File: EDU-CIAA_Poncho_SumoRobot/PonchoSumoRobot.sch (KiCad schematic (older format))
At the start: 26 parts, among them K1 RELAY_C, K2 RELAY_C, K3 RELAY_C, K4 RELAY_C, P1 CONN_01X02, P3 CONN_02X09, P4 CONN_01X02, P5 CONN_01X02, Q1 BC817-40, Q2 BC817-40, Q3 BC817-40, Q4 BC817-40

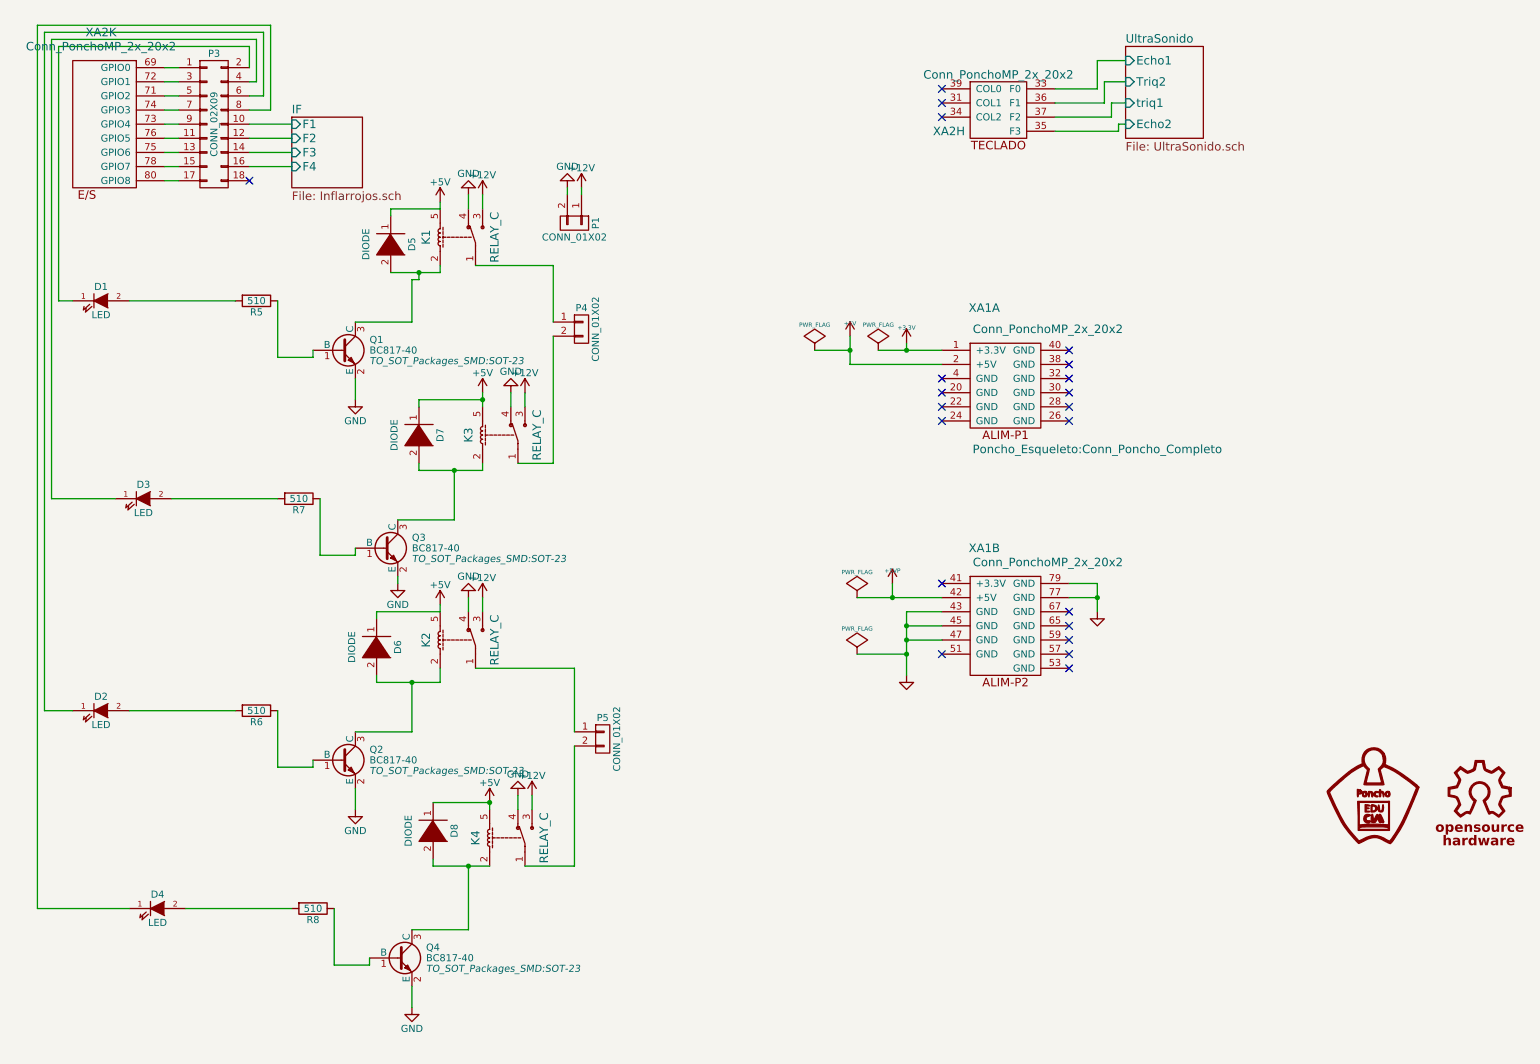
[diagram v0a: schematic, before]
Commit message: Reorganizo bibliotecas en esquemático y PCB. Reparo señal de 12V. Agrego Footprints. Coloco plantilla EDU-CIAA. Reparo asociación conector EDU-CIAA en sch y pcb.
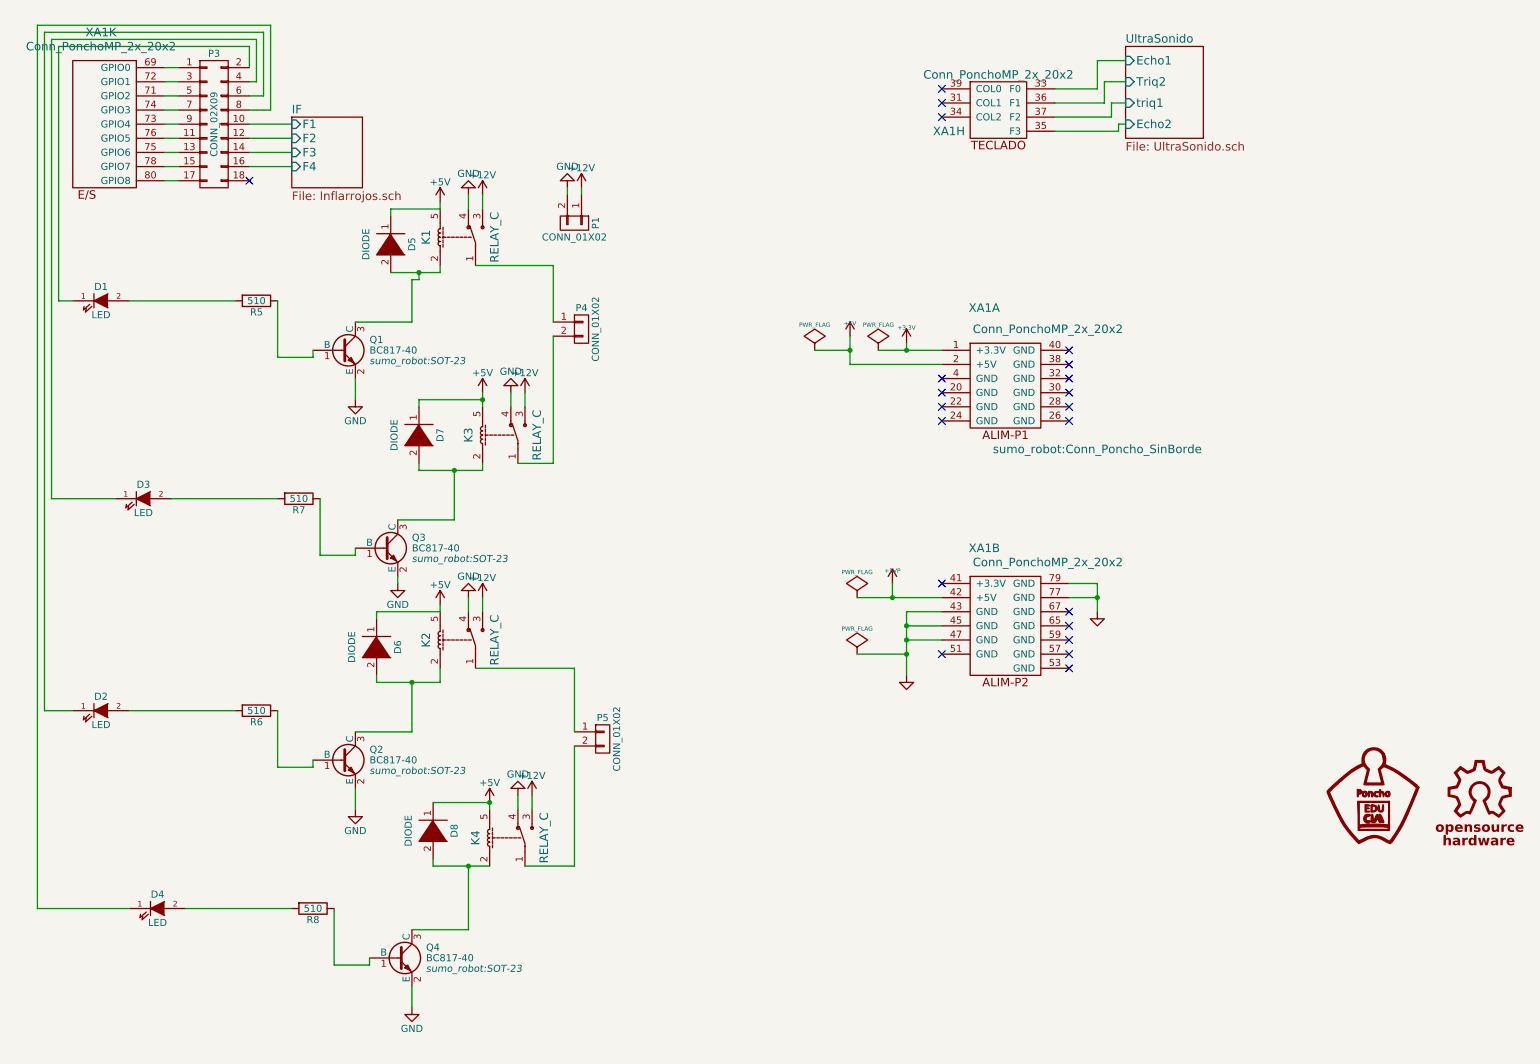
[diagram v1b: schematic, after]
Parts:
- D1, D2, D3, D4: footprint LEDs:LED_1206 -> sumo_robot:LED_1206
- D5, D6, D7, D8: footprint Diodes_ThroughHole:Diode_DO-41_SOD81_Horizontal_RM10 -> sumo_robot:Diode_DO-41_SOD81_Horizontal_RM10
- K1, K2, K3, K4: footprint Relays_ThroughHole:Relay_SANYOU_SRD_Series_Form_C -> sumo_robot:Relay_SANYOU_SRD_Series_Form_C
- P1, P4, P5: footprint Connect:bornier2 -> sumo_robot:bornier2
- P3: footprint Pin_Headers:Pin_Header_Straight_2x09 -> sumo_robot:Pin_Header_Straight_2x09
- Q1, Q2, Q3, Q4: footprint TO_SOT_Packages_SMD:SOT-23 -> sumo_robot:SOT-23
- R5, R6, R7, R8: footprint Resistors_ThroughHole:Resistor_Horizontal_RM7mm -> sumo_robot:Resistor_Horizontal_RM7mm
- XA1: footprint Poncho_Esqueleto:Conn_Poncho_Completo -> sumo_robot:Conn_Poncho_SinBorde
- XA1: renamed from XA2; footprint Poncho_Esqueleto:Conn_Poncho_Completo -> sumo_robot:Conn_Poncho_SinBorde
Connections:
- net +12V: now reaches K1.3
- net +12V: now also K2.3, K3.3, K4.3, P1.1 (P1)

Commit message: Correcciones propuestas al Poncho SumoRobot.
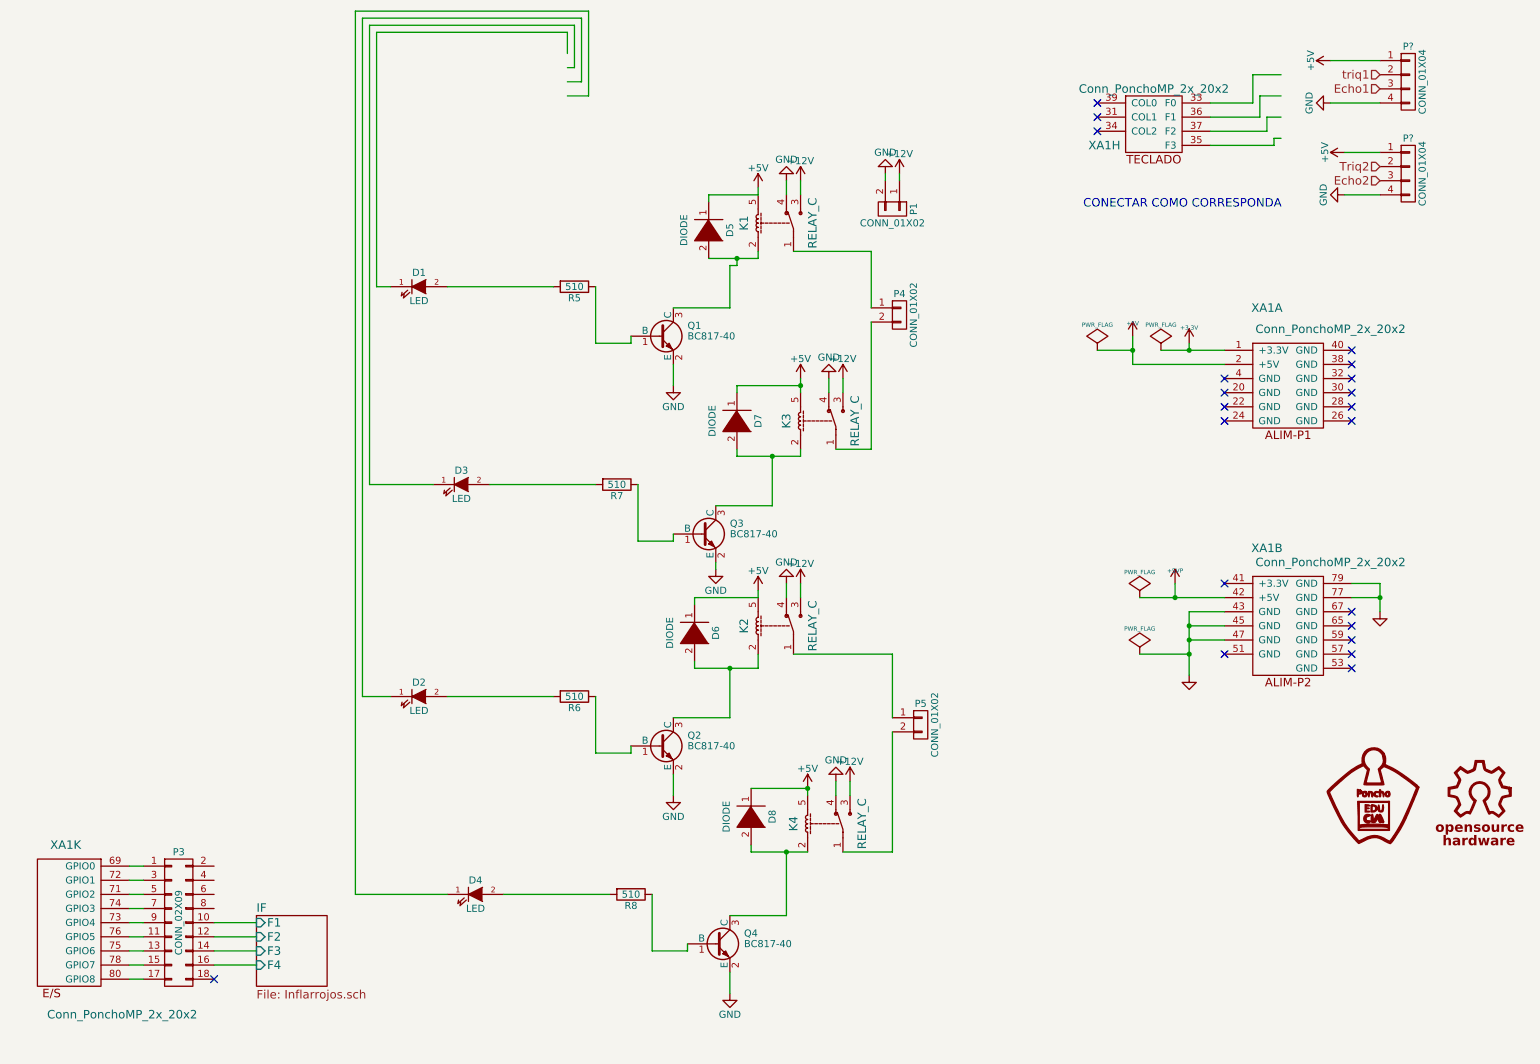
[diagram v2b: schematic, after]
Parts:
- added P? (x2): CONN_01X04, sumo_robot:Pin_Header_Straight_1x04, symbol CONN_01X04
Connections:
- net labels added: Echo1, Echo2, Triq2, triq1
- wire segments 128 -> 132
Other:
- note added: "CONECTAR COMO CORRESPONDA"
- moved on the sheet: D1, D2, D3, D4, D5, D6, D7, D8, K1, K2, K3, K4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

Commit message: Actualizo trabajo del Poncho Sumo Robot.
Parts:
- removed Q1, Q2, Q3, Q4: BC817-40, sumo_robot:SOT-23, symbol BC817-40
- added P7, P8: CONN_01X02, sumo_robot:Pin_Header_Straight_1x02, symbol CONN_01X02
- added Q1, Q2, Q3, Q4, Q5: 2SC1945, Power_Integrations:TO-220, symbol 2SC1945
- added R1, R2, R3, R4: 470, sumo_robot:Resistor_Horizontal_RM7mm, symbol R
- D1, D2, D3, D4: footprint sumo_robot:LED_1206 -> LEDs:LED-3MM
- gave numbers to parts that had none: 2
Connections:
- net labels removed: Echo1, Echo2, Triq2, triq1
- wire segments 132 -> 148
- no-connect marks 21 -> 20
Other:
- note removed: "CONECTAR COMO CORRESPONDA"
- moved on the sheet: D1, D2, D3, D4, D6, R5, R6, R7, R8

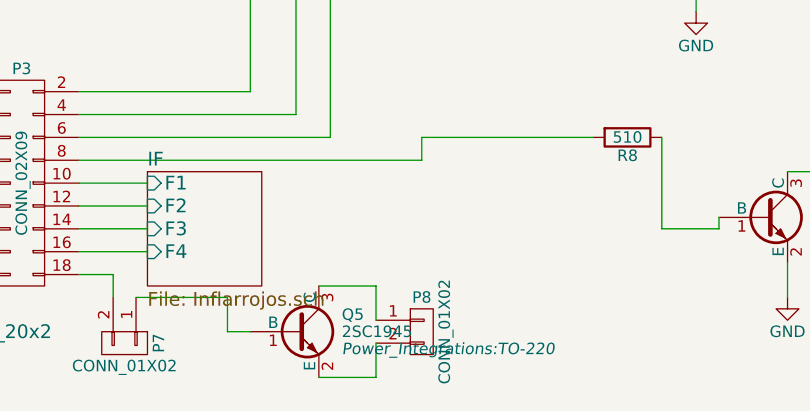
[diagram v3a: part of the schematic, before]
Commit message: EDU-CIAA Poncho Sumo Robot. Ultimos cambios de vías y puentes para simple faz.
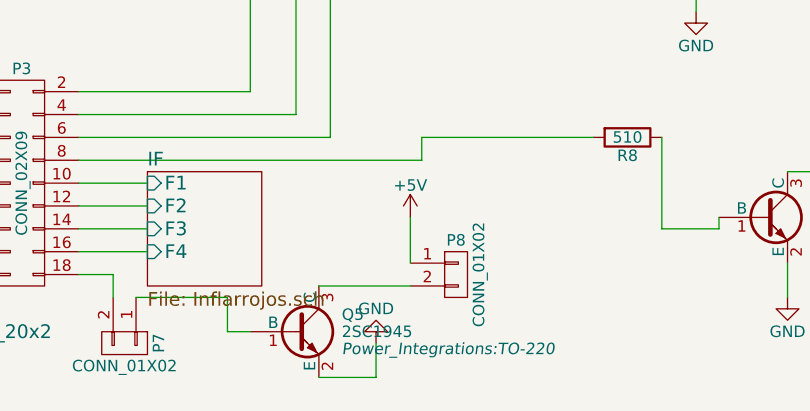
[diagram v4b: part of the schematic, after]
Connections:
- net +5V: now also P8.1 (P1)
- net at Q5.2 (E): no longer P8.2 (P2)
- net at Q5.3 (C): now also P8.2 (P2); no longer P8.1 (P1)
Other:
- moved on the sheet: P8
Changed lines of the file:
@@
 L CONN_01X02 P8
 U 1 1 579758C5
-P 3350 7550
-F 0 "P8" H 3350 7700 50  0000 C CNN
-F 1 "CONN_01X02" V 3450 7550 50  0000 C CNN
-F 2 "sumo_robot:Pin_Header_Straight_1x02" H 3350 7550 50  0001 C CNN
-F 3 "" H 3350 7550 50  0000 C CNN
-	1    3350 7550
+P 3500 7300
+F 0 "P8" H 3500 7450 50  0000 C CNN
+F 1 "CONN_01X02" V 3600 7300 50  0000 C CNN
+F 2 "sumo_robot:Pin_Header_Straight_1x02" H 3500 7300 50  0001 C CNN
+F 3 "" H 3500 7300 50  0000 C CNN
+	1    3500 7300
 	1    0    0    -1
 $EndComp
 Wire Wire Line
-	2900 7350 3150 7350
-Wire Wire Line
-	3150 7350 3150 7500
+	2900 7350 3300 7350
 Wire Wire Line
 	2900 7750 3150 7750
@@
 	1    0    0    -1
 $EndComp
+$Comp
+L GND #PWR032
+U 1 1 57C05FB0
+P 3150 7600
+F 0 "#PWR032" H 3150 7350 50  0001 C CNN
+F 1 "GND" H 3150 7450 50  0000 C CNN
+F 2 "" H 3150 7600 50  0000 C CNN
+F 3 "" H 3150 7600 50  0000 C CNN
+	1    3150 7600
+	-1   0    0    1
+$EndComp
+Wire Wire Line
+	3300 7250 3300 7050
+$Comp
+L +5V #PWR033
+U 1 1 57C0637D
+P 3300 7050
+F 0 "#PWR033" H 3300 6900 50  0001 C CNN
+F 1 "+5V" H 3300 7190 50  0000 C CNN
+F 2 "" H 3300 7050 50  0000 C CNN
+F 3 "" H 3300 7050 50  0000 C CNN
+	1    3300 7050
+	1    0    0    -1
+$EndComp
